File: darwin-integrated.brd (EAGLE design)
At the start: 96 x 62 mm, 41 parts

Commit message: DRC related cleanup.
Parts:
- moved C13 0.31 mm to (55.7, 20.5)
- moved C14 0.20 mm to (77.0, 32.8)
- moved C3 0.05 mm to (65.4, 48.6)
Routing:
- net USB_HOSTEN: track 6.64 -> 0.00 mm
- net GND: track 86.3 -> 91.4 mm, vias 42 -> 44
- net 3V3: track 63.1 -> 64.6 mm

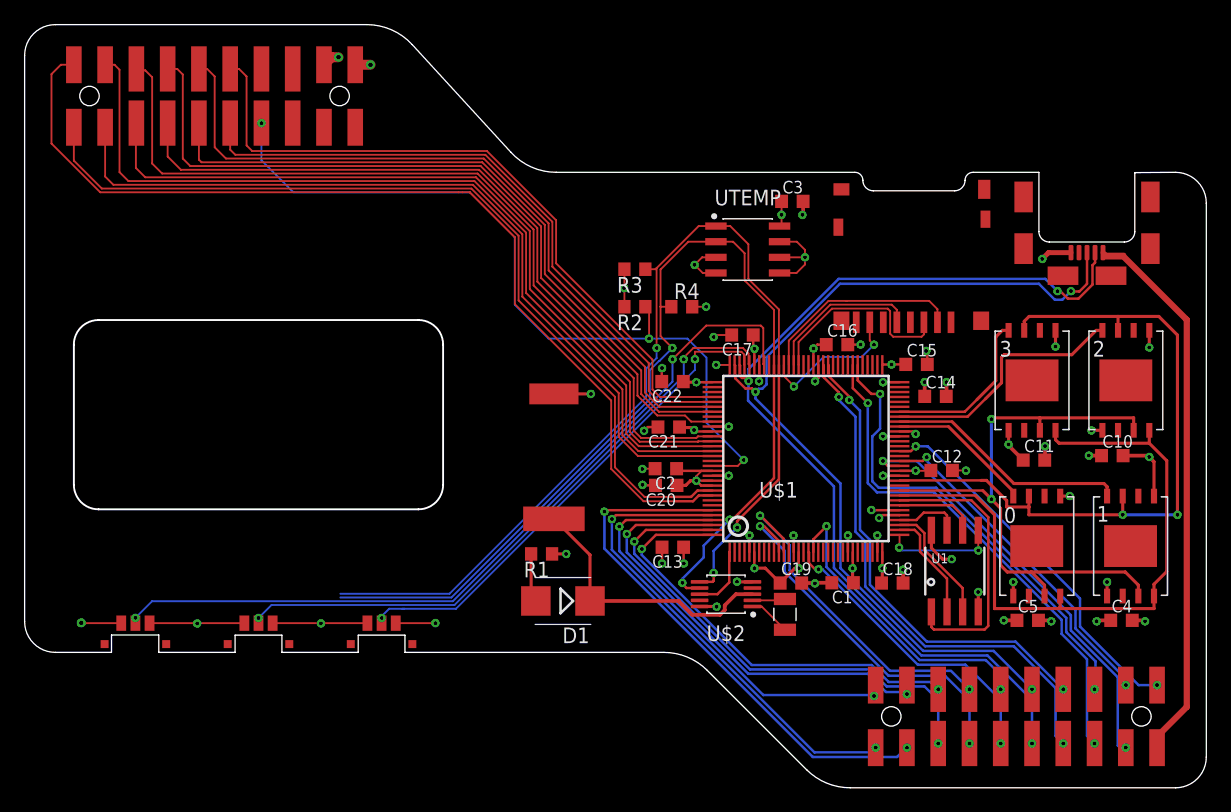
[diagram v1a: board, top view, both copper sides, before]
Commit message: Silk cleanup and other housecleaning.
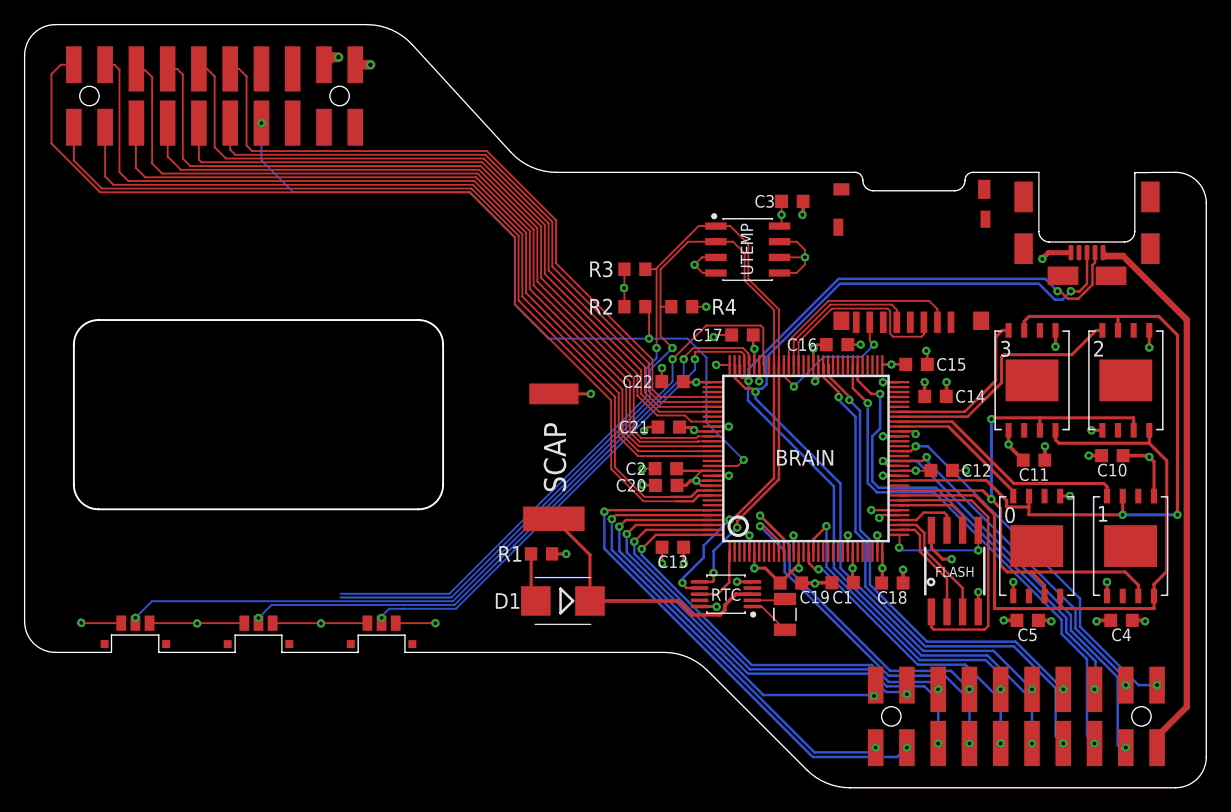
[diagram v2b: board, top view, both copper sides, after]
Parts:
- renumbered U$1 to BRAIN, U$2 to RTC, U1 to FLASH
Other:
- board text added: "SCAP"

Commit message: Added screen contacts
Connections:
- net 3V3: now also U$10.P0
- net CORE_SCL: now also U$10.P2
- net CORE_SDA: now also U$10.P3
- net GND: now also U$10.P1
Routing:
- net CORE_SDA: track 84.5 -> 95.8 mm, vias 3 -> 5
- net CORE_SCL: track 85.3 -> 94.7 mm
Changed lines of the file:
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@@
 <setting verticaltext="up"/>
 </settings>
-<grid distance="0.1" unitdist="mm" unit="mm" style="lines" multiple="1" display="no" altdistance="0.1" altunitdist="mm" altunit="mm"/>
+<grid distance="6" unitdist="mil" unit="mil" style="lines" multiple="1" display="no" altdistance="0.1" altunitdist="mm" altunit="mm"/>
 <layers>
 <layer number="1" name="Top" color="4" fill="1" visible="yes" active="yes"/>
 <layer number="2" name="PWR" color="16" fill="3" visible="no" active="yes"/>
-<layer number="15" name="GND" color="23" fill="4" visible="no" active="yes"/>
+<layer number="15" name="GND" color="23" fill="4" visible="yes" active="yes"/>
 <layer number="16" name="Bottom" color="1" fill="1" visible="yes" active="yes"/>
 <layer number="17" name="Pads" color="2" fill="1" visible="yes" active="yes"/>
@@
 <wire x1="58.8906625" y1="17.73215" x2="57.83975" y2="17.73215" width="0.2032" layer="1"/>
 <wire x1="64.28" y1="35.35" x2="64.28" y2="26.0561" width="0.2032" layer="1"/>
-<wire x1="64.28" y1="26.0561" x2="61.11195" y2="22.88805" width="0.2032" layer="1"/>
-<wire x1="61.11195" y1="22.88805" x2="61.06895" y2="22.84505" width="0.2032" layer="1"/>
-<wire x1="61.06895" y1="22.84505" x2="60.881" y2="22.6571" width="0.2032" layer="1"/>
+<wire x1="64.28" y1="26.0561" x2="60.881" y2="22.6571" width="0.2032" layer="1"/>
 <wire x1="60.881" y1="22.6571" x2="60.881" y2="22.144" width="0.2032" layer="1"/>
 <via x="60.881" y="22.144" extent="1-16" drill="0.3"/>
@@
 <wire x1="58.976" y1="17.8174875" x2="58.8906625" y2="17.73215" width="0.2032" layer="1"/>
 <via x="54.3407625" y="36.7284" extent="1-16" drill="0.3"/>
-<wire x1="54.3407625" y1="36.7284" x2="54.3407625" y2="35.9076125" width="0.1524" layer="16"/>
-<wire x1="53.4924" y1="32.739859375" x2="37.516540625" y2="16.764" width="0.1524" layer="16"/>
-<wire x1="37.516540625" y1="16.764" x2="28.6512" y2="16.764" width="0.1524" layer="16"/>
-<wire x1="54.3407625" y1="35.9076125" x2="53.4924" y2="35.05925" width="0.1524" layer="16"/>
-<wire x1="53.4924" y1="35.05925" x2="53.4924" y2="32.739859375" width="0.1524" layer="16"/>
 <contactref element="UTEMP" pad="1"/>
 <wire x1="61.7982" y1="42.3418" x2="61.7982" y2="45.1612" width="0.1524" layer="1"/>
@@
 <wire x1="53.428" y1="43.1292" x2="54.2544" y2="43.1292" width="0.1524" layer="1"/>
 <wire x1="54.2544" y1="43.1292" x2="54.3407625" y2="43.2155625" width="0.1524" layer="1"/>
+<contactref element="U$10" pad="P3"/>
+<wire x1="18.41" y1="47.73" x2="18.4116" y2="47.73" width="0.1524" layer="16"/>
+<wire x1="20.4216" y1="45.72" x2="18.4116" y2="47.73" width="0.1524" layer="16"/>
+<via x="20.4216" y="45.72" extent="1-16" drill="0.35"/>
+<wire x1="20.4216" y1="45.72" x2="33.528" y2="45.72" width="0.1524" layer="1"/>
+<wire x1="33.528" y1="45.72" x2="35.052" y2="44.196" width="0.1524" layer="1"/>
+<via x="35.052" y="44.196" extent="1-16" drill="0.35"/>
+<wire x1="35.052" y1="44.196" x2="35.5092" y2="43.7388" width="0.1524" layer="16"/>
+<wire x1="35.5092" y1="43.7388" x2="35.5092" y2="42.95065625" width="0.1524" layer="16"/>
+<wire x1="48.13225625" y1="30.3276" x2="49.40374375" y2="30.3276" width="0.1524" layer="16"/>
+<wire x1="53.8984" y1="34.82225625" x2="53.8984" y2="35.46525" width="0.1524" layer="16"/>
+<wire x1="54.3407625" y1="35.9076125" x2="54.3407625" y2="36.7284" width="0.1524" layer="16"/>
+<wire x1="53.8984" y1="35.46525" x2="54.3407625" y2="35.9076125" width="0.1524" layer="16"/>
+<wire x1="35.5092" y1="42.95065625" x2="48.13225625" y2="30.3276" width="0.1524" layer="16"/>
+<wire x1="49.40374375" y1="30.3276" x2="53.8984" y2="34.82225625" width="0.1524" layer="16"/>
 </signal>
 <signal name="CORE_SCL">
@@
 <wire x1="56.3486" y1="17.6482" x2="56.436" y2="17.6482" width="0.2032" layer="1"/>
 <via x="55.626" y="36.7284" extent="1-16" drill="0.3"/>
-<wire x1="55.626" y1="36.7284" x2="54.5774" y2="35.6798" width="0.1524" layer="16"/>
-<wire x1="54.5774" y1="35.6798" x2="54.54400625" y2="35.6798" width="0.1524" layer="16"/>
-<wire x1="37.66894375" y1="16.4592" x2="28.6512" y2="16.4592" width="0.1524" layer="16"/>
-<wire x1="53.7972" y1="32.58745625" x2="37.66894375" y2="16.4592" width="0.1524" layer="16"/>
-<wire x1="54.54400625" y1="35.6798" x2="53.7972" y2="34.93299375" width="0.1524" layer="16"/>
-<wire x1="53.7972" y1="34.93299375" x2="53.7972" y2="32.58745625" width="0.1524" layer="16"/>
 <contactref element="UTEMP" pad="2"/>
 <wire x1="63.88" y1="39.82894375" x2="61.4934" y2="42.21554375" width="0.1524" layer="1"/>
@@
 <contactref element="R4" pad="1"/>
 <wire x1="55.538" y1="40.0812" x2="54.6608" y2="40.0812" width="0.1524" layer="1"/>
+<contactref element="U$10" pad="P2"/>
+<wire x1="20.95" y1="47.73" x2="21.05766875" y2="47.73" width="0.1524" layer="16"/>
+<wire x1="21.05766875" y1="47.73" x2="22.23876875" y2="48.9111" width="0.1524" layer="16"/>
+<wire x1="22.23876875" y1="48.9111" x2="29.1177" y2="48.9111" width="0.1524" layer="16"/>
+<wire x1="29.1177" y1="48.9111" x2="48.006" y2="30.0228" width="0.1524" layer="16"/>
+<wire x1="48.006" y1="30.0228" x2="49.53" y2="30.0228" width="0.1524" layer="16"/>
+<wire x1="49.53" y1="30.0228" x2="54.2032" y2="34.696" width="0.1524" layer="16"/>
+<wire x1="54.2032" y1="34.696" x2="54.2032" y2="35.33899375" width="0.1524" layer="16"/>
+<wire x1="55.59260625" y1="36.7284" x2="54.2032" y2="35.33899375" width="0.1524" layer="16"/>
+<wire x1="55.59260625" y1="36.7284" x2="55.626" y2="36.7284" width="0.1524" layer="16"/>
 </signal>
 <signal name="GPS_TX">
@@
 <wire x1="57.5646" y1="25.9466" x2="57.5646" y2="26.3146" width="0.1524" layer="1"/>
 <wire x1="57.5646" y1="26.3146" x2="58" y2="26.75" width="0.1524" layer="1"/>
+<contactref element="U$10" pad="P0"/>
 </signal>
 <signal name="GND">
@@
 <wire x1="7.625" y1="14.375" x2="7.6" y2="14.4" width="0.1524" layer="1"/>
 <via x="7.6" y="14.4" extent="1-16" drill="0.3"/>
+<contactref element="U$10" pad="P1"/>
 </signal>
 <signal name="N$1">

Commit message: Routing Tweaks
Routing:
- net CORE_SDA: vias 5 -> 4
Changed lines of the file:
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@@
 <layer number="1" name="Top" color="4" fill="1" visible="yes" active="yes"/>
 <layer number="2" name="PWR" color="16" fill="3" visible="no" active="yes"/>
-<layer number="15" name="GND" color="23" fill="4" visible="yes" active="yes"/>
+<layer number="15" name="GND" color="23" fill="4" visible="no" active="yes"/>
 <layer number="16" name="Bottom" color="1" fill="1" visible="yes" active="yes"/>
 <layer number="17" name="Pads" color="2" fill="1" visible="yes" active="yes"/>
@@
 <wire x1="54.2544" y1="43.1292" x2="54.3407625" y2="43.2155625" width="0.1524" layer="1"/>
 <contactref element="U$10" pad="P3"/>
-<wire x1="18.41" y1="47.73" x2="18.4116" y2="47.73" width="0.1524" layer="16"/>
-<wire x1="20.4216" y1="45.72" x2="18.4116" y2="47.73" width="0.1524" layer="16"/>
-<via x="20.4216" y="45.72" extent="1-16" drill="0.35"/>
-<wire x1="20.4216" y1="45.72" x2="33.528" y2="45.72" width="0.1524" layer="1"/>
-<wire x1="33.528" y1="45.72" x2="35.052" y2="44.196" width="0.1524" layer="1"/>
+<wire x1="32.766" y1="46.482" x2="35.052" y2="44.196" width="0.1524" layer="1"/>
 <via x="35.052" y="44.196" extent="1-16" drill="0.35"/>
 <wire x1="35.052" y1="44.196" x2="35.5092" y2="43.7388" width="0.1524" layer="16"/>
@@
 <wire x1="35.5092" y1="42.95065625" x2="48.13225625" y2="30.3276" width="0.1524" layer="16"/>
 <wire x1="49.40374375" y1="30.3276" x2="53.8984" y2="34.82225625" width="0.1524" layer="16"/>
+<wire x1="18.41" y1="47.73" x2="19.658" y2="46.482" width="0.1524" layer="1"/>
+<wire x1="19.658" y1="46.482" x2="32.766" y2="46.482" width="0.1524" layer="1"/>
 </signal>
 <signal name="CORE_SCL">
